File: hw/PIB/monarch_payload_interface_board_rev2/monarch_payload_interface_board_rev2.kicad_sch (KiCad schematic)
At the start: 0 parts

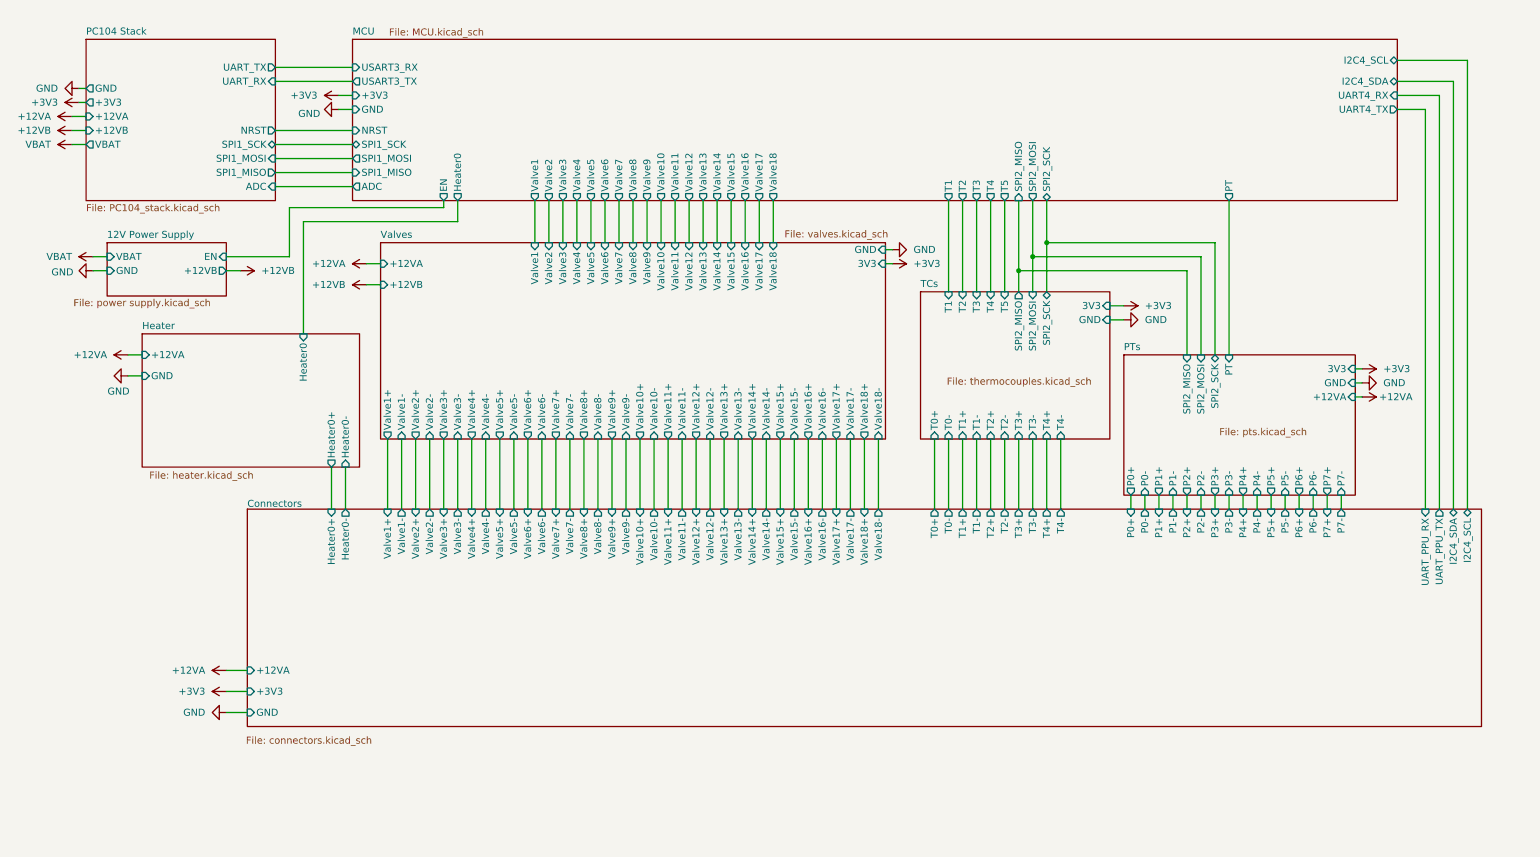
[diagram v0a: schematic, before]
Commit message: Schematic Updates Finished -> AD7124 Voltage Reading Fix + Connector Linkage Issue Fix
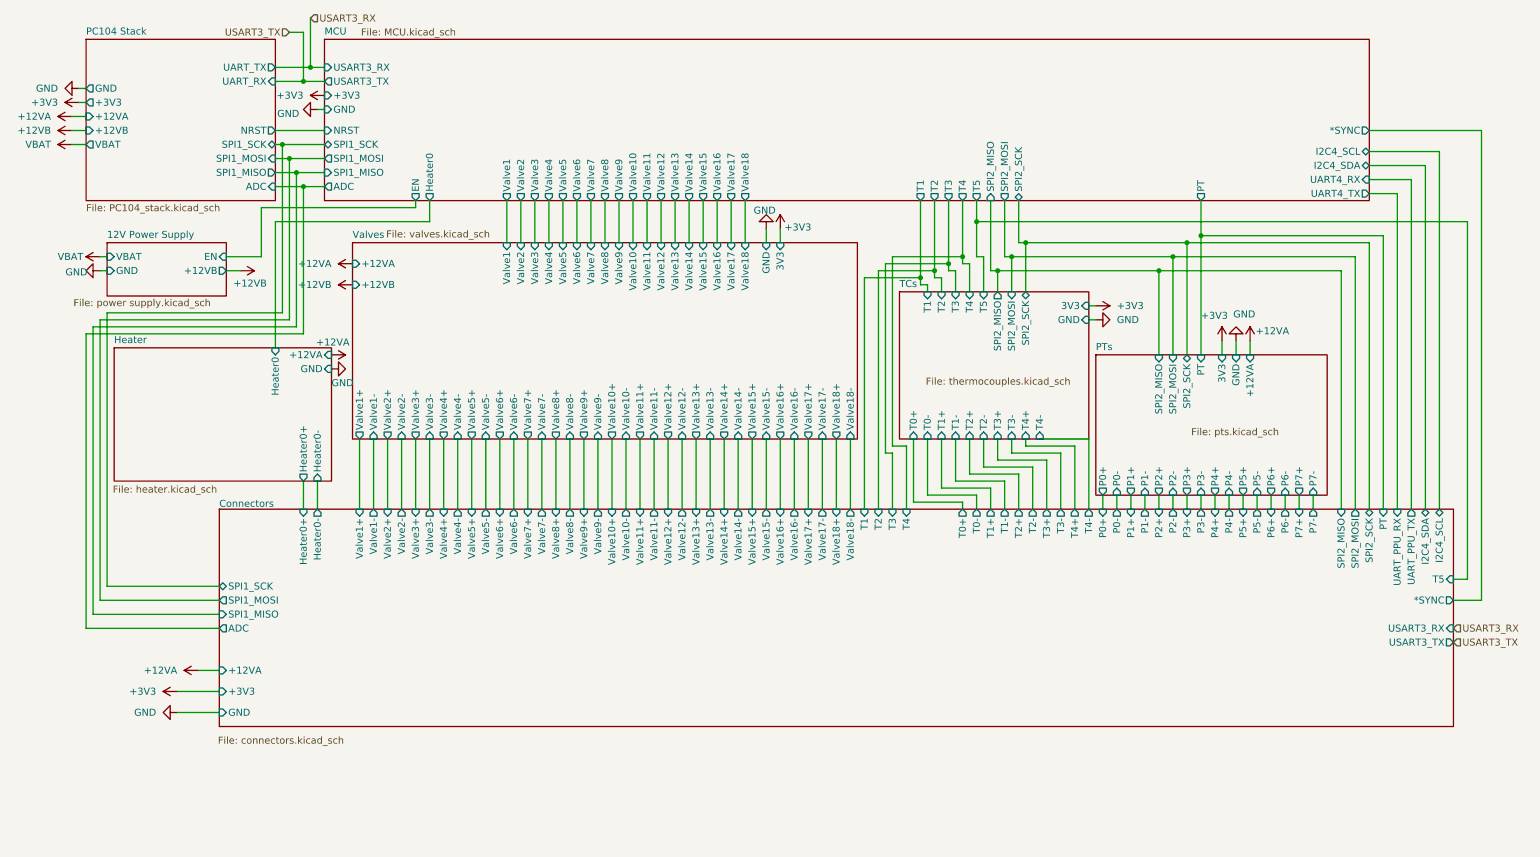
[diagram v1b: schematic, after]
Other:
- sheet Connectors ports: added *SYNC, ADC, PT, SPI1_MISO, SPI1_MOSI, SPI1_SCK, SPI2_MISO, SPI2_MOSI, SPI2_SCK, T1, T2, T3, T4, T5, USART3_RX, USART3_TX; removed none
- sheet MCU ports: added *SYNC; removed none

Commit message: Layout Rev Done - NO DRC Check
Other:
- sheet PC104 Stack ports: added *SYNC; removed none
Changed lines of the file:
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@@
 	)
 	(junction
+		(at 278.13 119.38)
+		(diameter 0)
+		(color 0 0 0 0)
+	)
+	(junction
 		(at 190.5 59.69)
 		(diameter 0)
@@
 	(wire
 		(pts
+			(xy 20.32 151.13) (xy 278.13 151.13)
+		)
+		(stroke
+			(width 0)
+			(type default)
+		)
+	)
+	(wire
+		(pts
 			(xy 242.57 100.33) (xy 242.57 102.87)
 		)
@@
 	(wire
 		(pts
+			(xy 278.13 151.13) (xy 278.13 119.38)
+		)
+		(stroke
+			(width 0)
+			(type default)
+		)
+	)
+	(wire
+		(pts
 			(xy 59.69 34.29) (xy 68.58 34.29)
 		)
@@
 	(wire
 		(pts
+			(xy 25.4 43.18) (xy 20.32 43.18)
+		)
+		(stroke
+			(width 0)
+			(type default)
+		)
+	)
+	(wire
+		(pts
 			(xy 63.5 87.63) (xy 64.77 87.63)
 		)
@@
 	(wire
 		(pts
+			(xy 20.32 43.18) (xy 20.32 151.13)
+		)
+		(stroke
+			(width 0)
+			(type default)
+		)
+	)
+	(wire
+		(pts
 			(xy 194.31 96.52) (xy 194.31 102.87)
 		)
@@
 			)
 		)
+		(pin "*SYNC" input
+			(at 25.4 43.18 180)
+			(effects
+				(font
+					(size 1.27 1.27)
+				)
+				(justify left)
+			)
+		)

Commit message: Schematic Unconnected Fix
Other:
- sheet Valves ports: added none; removed 3V3
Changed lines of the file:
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@@
 	(wire
 		(pts
-			(xy 151.13 64.77) (xy 151.13 67.31)
-		)
-		(stroke
-			(width 0)
-			(type default)
-		)
-	)
-	(wire
-		(pts
 			(xy 130.81 102.87) (xy 130.81 115.57)
 		)
@@
 	(wire
 		(pts
+			(xy 64.77 29.21) (xy 281.94 29.21)
+		)
+		(stroke
+			(width 0)
+			(type default)
+		)
+	)
+	(wire
+		(pts
 			(xy 137.16 59.69) (xy 137.16 67.31)
 		)
@@
 	(wire
 		(pts
+			(xy 281.94 139.7) (xy 273.05 139.7)
+		)
+		(stroke
+			(width 0)
+			(type default)
+		)
+	)
+	(wire
+		(pts
 			(xy 138.43 102.87) (xy 138.43 115.57)
 		)
@@
 	(wire
 		(pts
+			(xy 281.94 29.21) (xy 281.94 139.7)
+		)
+		(stroke
+			(width 0)
+			(type default)
+		)
+	)
+	(wire
+		(pts
 			(xy 64.77 100.33) (xy 64.77 95.25)
 		)
@@
 	(wire
 		(pts
+			(xy 280.67 137.16) (xy 273.05 137.16)
+		)
+		(stroke
+			(width 0)
+			(type default)
+		)
+	)
+	(wire
+		(pts
 			(xy 219.71 72.39) (xy 252.73 72.39)
 		)
@@
 	(wire
 		(pts
+			(xy 66.04 26.67) (xy 280.67 26.67)
+		)
+		(stroke
+			(width 0)
+			(type default)
+		)
+	)
+	(wire
+		(pts
 			(xy 219.71 113.03) (xy 219.71 115.57)
 		)
@@
 	(wire
 		(pts
-			(xy 62.23 29.21) (xy 64.77 29.21)
-		)
-		(stroke
-			(width 0)
-			(type default)
-		)
-	)
-	(wire
-		(pts
 			(xy 168.91 72.39) (xy 168.91 115.57)
 		)
@@
 	(wire
 		(pts
+			(xy 280.67 26.67) (xy 280.67 137.16)
+		)
+		(stroke
+			(width 0)
+			(type default)
+		)
+	)
+	(wire
+		(pts
 			(xy 133.35 102.87) (xy 133.35 115.57)
 		)
@@
 		)
 	)
-	(hierarchical_label "USART3_RX"
-		(shape input)
-		(at 273.05 137.16 0)
-		(effects
-			(font
-				(size 1.27 1.27)
-			)
-			(justify left)
-		)
-	)
-	(hierarchical_label "USART3_TX"
-		(shape input)
-		(at 62.23 29.21 180)
-		(effects
-			(font
-				(size 1.27 1.27)
-			)
-			(justify right)
-		)
-	)
-	(hierarchical_label "USART3_RX"
-		(shape input)
-		(at 66.04 26.67 0)
-		(effects
-			(font
-				(size 1.27 1.27)
-			)
-			(justify left)
-		)
-	)
-	(hierarchical_label "USART3_TX"
-		(shape input)
-		(at 273.05 139.7 0)
-		(effects
-			(font
-				(size 1.27 1.27)
-			)
-			(justify left)
-		)
-	)
 	(symbol
 		(lib_id "power:+3V3")
@@
 	(symbol
 		(lib_id "power:+3V3")
-		(at 151.13 64.77 0)
-		(unit 1)
-		(body_style 1)
-		(exclude_from_sim no)
-		(in_bom yes)
-		(on_board yes)
-		(in_pos_files yes)
-		(dnp no)
-		(property "Reference" "#PWR06"
-			(at 151.13 68.58 0)
-			(hide yes)
-			(show_name no)
-			(do_not_autoplace no)
-			(effects
-				(font
-					(size 1.27 1.27)
-				)
-			)
-		)
-		(property "Value" "+3V3"
-			(at 151.892 64.516 0)
-			(show_name no)
-			(do_not_autoplace no)
-			(effects
-				(font
-					(size 1.27 1.27)
-				)
-				(justify left)
-			)
-		)
-		(property "Footprint" ""
-			(at 151.13 64.77 0)
-			(hide yes)
-			(show_name no)
-			(do_not_autoplace no)
-			(effects
-				(font
-					(size 1.27 1.27)
-				)
-			)
-		)
-		(property "Datasheet" ""
-			(at 151.13 64.77 0)
-			(hide yes)
-			(show_name no)
-			(do_not_autoplace no)
-			(effects
-				(font
-					(size 1.27 1.27)
-				)
-			)
-		)
-		(property "Description" "Power symbol creates a global label with name \"+3V3\""
-			(at 151.13 64.77 0)
-			(hide yes)
-			(show_name no)
-			(do_not_autoplace no)
-			(effects
-				(font
-					(size 1.27 1.27)
-				)
-			)
-		)
-		(pin "1"
-		)
-		(instances
-			(project "monarch_payload_interface_board_rev2"
-				(path "/bf7ee58d-ac53-49d1-a6b2-96a87d67b737"
-					(reference "#PWR06")
-					(unit 1)
-				)
-			)
-		)
-	)
-	(symbol
-		(lib_id "power:+3V3")
 		(at 231.14 85.09 0)
 		(unit 1)
@@
 			)
 		)
-		(pin "3V3" input
-			(at 151.13 67.31 90)
-			(effects
-				(font
-					(size 1.27 1.27)
-				)
-				(justify right)
-			)
-		)
